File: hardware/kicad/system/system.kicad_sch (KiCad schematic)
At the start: 0 parts

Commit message: system: connected top sheet for the integrated PCB
Rebuild system.kicad_sch as the netlist-connected 5-board hierarchy
(motor_power, motor_feedback, mppt_buck, boost_v2_mill, c2000_feedback),
replacing the old block-diagram. Connectivity by global labels.

- J_ARD (Arduino), J_C2K (C2000), J_INA (PV INA219) connectors
- external screw terminals: 3-phase, motor, PV, store, load, +15V, +5V
- 17 diagnostic probe-point headers on the key nets
- single GND<->GND_MCU star tie (R_STAR 0R)
- generator tools/generators/build_system_top.py (reference; the sheet is
  now hand-maintained in the GUI)

Netlist verified: all 36 top-level connector pins match the interface
contract, no shorts, STORE/V1/LOAD buses span the right boards. Sub-sheet
.kicad_sch carry hierarchical instance data from opening the hierarchy.
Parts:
- added J_15V: +15V gate supply, symbol Connector:Screw_Terminal_01x02
- added J_3PH: 3-phase in, symbol Connector:Screw_Terminal_01x03
- added J_5V: +5V supply, symbol Connector:Screw_Terminal_01x02
- added J_ARD: Arduino Nano, symbol Connector_Generic:Conn_01x06
- added J_C2K: C2000 LaunchPad, symbol Connector_Generic:Conn_01x07
- added J_INA: PV INA219, symbol Connector_Generic:Conn_01x06
- added J_LOAD: pulsing load, symbol Connector:Screw_Terminal_01x02
- added J_MOT: DC motor, symbol Connector:Screw_Terminal_01x02
- added J_PV: PV panel, symbol Connector:Screw_Terminal_01x02
- added J_STO: 1F store, symbol Connector:Screw_Terminal_01x02
- added R_STAR: 0R, symbol Device:R
- added TP1: V1, symbol Connector:TestPoint
- added TP10: PWM_BOOST, symbol Connector:TestPoint
- added TP11: PWM_MPPT, symbol Connector:TestPoint
- added TP12: ADC_V1, symbol Connector:TestPoint
- added TP13: ADC_LOAD, symbol Connector:TestPoint
- added TP14: ADC_STORE, symbol Connector:TestPoint
- added TP15: MCU_V1, symbol Connector:TestPoint
- added TP16: PV_SDA, symbol Connector:TestPoint
- added TP17: PV_SCL, symbol Connector:TestPoint
- added TP2: STORE, symbol Connector:TestPoint
- added TP3: LOAD, symbol Connector:TestPoint
- added TP4: +5V_PWR, symbol Connector:TestPoint
- added TP5: +3V3, symbol Connector:TestPoint
- added TP6: +15V_GATE, symbol Connector:TestPoint
- added TP7: GND, symbol Connector:TestPoint
- added TP8: GND_MCU, symbol Connector:TestPoint
- added TP9: PWM_MOTOR, symbol Connector:TestPoint
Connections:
- new net +15V_GATE: J_15V.1 (Pin_1), TP6.1
- new net +3V3: J_C2K.6 (Pin_6), TP5.1
- new net +5V_PWR: J_5V.1 (Pin_1), J_ARD.5 (Pin_5), J_INA.3 (Pin_3), TP4.1
- new net 3PH_U: J_3PH.1 (Pin_1)
- new net 3PH_V: J_3PH.2 (Pin_2)
- new net 3PH_W: J_3PH.3 (Pin_3)
- new net ADC_LOAD: J_C2K.2 (Pin_2), TP13.1
- new net ADC_STORE: J_C2K.3 (Pin_3), TP14.1
- new net ADC_V1: J_C2K.1 (Pin_1), TP12.1
- new net GND: J_15V.2 (Pin_2), J_5V.2 (Pin_2), J_ARD.6 (Pin_6), J_C2K.7 (Pin_7), J_INA.4 (Pin_4), J_LOAD.2 (Pin_2), J_PV.2 (Pin_2), J_STO.2 (Pin_2), R_STAR.1, TP7.1
- new net GND_MCU: R_STAR.2, TP8.1
- new net LOAD: J_LOAD.1 (Pin_1), TP3.1
- new net MCU_V1: J_ARD.1 (Pin_1), TP15.1
- new net MOTOR_A: J_MOT.1 (Pin_1)
- new net MOTOR_B: J_MOT.2 (Pin_2)
- new net PV_BUCK_IN: J_INA.2 (Pin_2)
- new net PV_PLUS: J_INA.1 (Pin_1), J_PV.1 (Pin_1)
- new net PV_SCL: J_ARD.3 (Pin_3), J_INA.6 (Pin_6), TP17.1
- new net PV_SDA: J_ARD.2 (Pin_2), J_INA.5 (Pin_5), TP16.1
- new net PWM_BOOST: J_C2K.5 (Pin_5), TP10.1
- new net PWM_MOTOR: J_C2K.4 (Pin_4), TP9.1
- new net PWM_MPPT: J_ARD.4 (Pin_4), TP11.1
- new net STORE: J_STO.1 (Pin_1), TP2.1
- new net V1: TP1.1
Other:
- removed sheet Buck
- removed sheet Current sense
- removed sheet Feedback
- removed sheet MPPT + PV
- removed sheet Motor-drive
- removed sheet Rectifier
- added sheet C2000 Feedback (../boards/c2000_feedback/c2000_feedback.kicad_sch)
- added sheet MPPT buck (../boards/mppt_buck/mppt_buck.kicad_sch)
- added sheet Motor Feedback (../boards/motor_feedback/motor_feedback.kicad_sch)
- added sheet Motor Power (../boards/motor_power/motor_power.kicad_sch)
- sheet Boost: file ../boards/boost/boost.kicad_sch -> ../boards/boost/boost_v2_mill/boost_v2_mill.kicad_sch
- sheet Boost ports: added +15V_GATE, GND, GND_MCU, LOAD, PWM_BOOST, STORE; removed none
- note removed: "+ 3x transformer (eksterne)"
- note removed: "+ overvaagning (PC)"
- note removed: "1F LAGER"
- note removed: "3-fase"
- note removed: "5 V"
- note removed: "5 V fra lager"
- note removed: "ADC"
- note removed: "ARDUINO UNO"
- note removed: "DC-motor + AC-generator"
- note removed: "Feedback/current sense maaler V1, V2, V3 + gren-stroemme"
- note removed: "PID: V1 via motor-PWM"
- note removed: "PULSERENDE LAST"
- note removed: "PWM (PID regulerer V1 via motorfart)"
- note removed: "V1 = 15 V"
- note removed: "V2 = 10 V"
- note removed: "V3 (PV-energi bruges foerst)"
- note removed: "V3 = 5 V"
- note removed: "motorkabel (M1)"
- title: 62768 Electrical Energy Systems - samlet system -> (none)

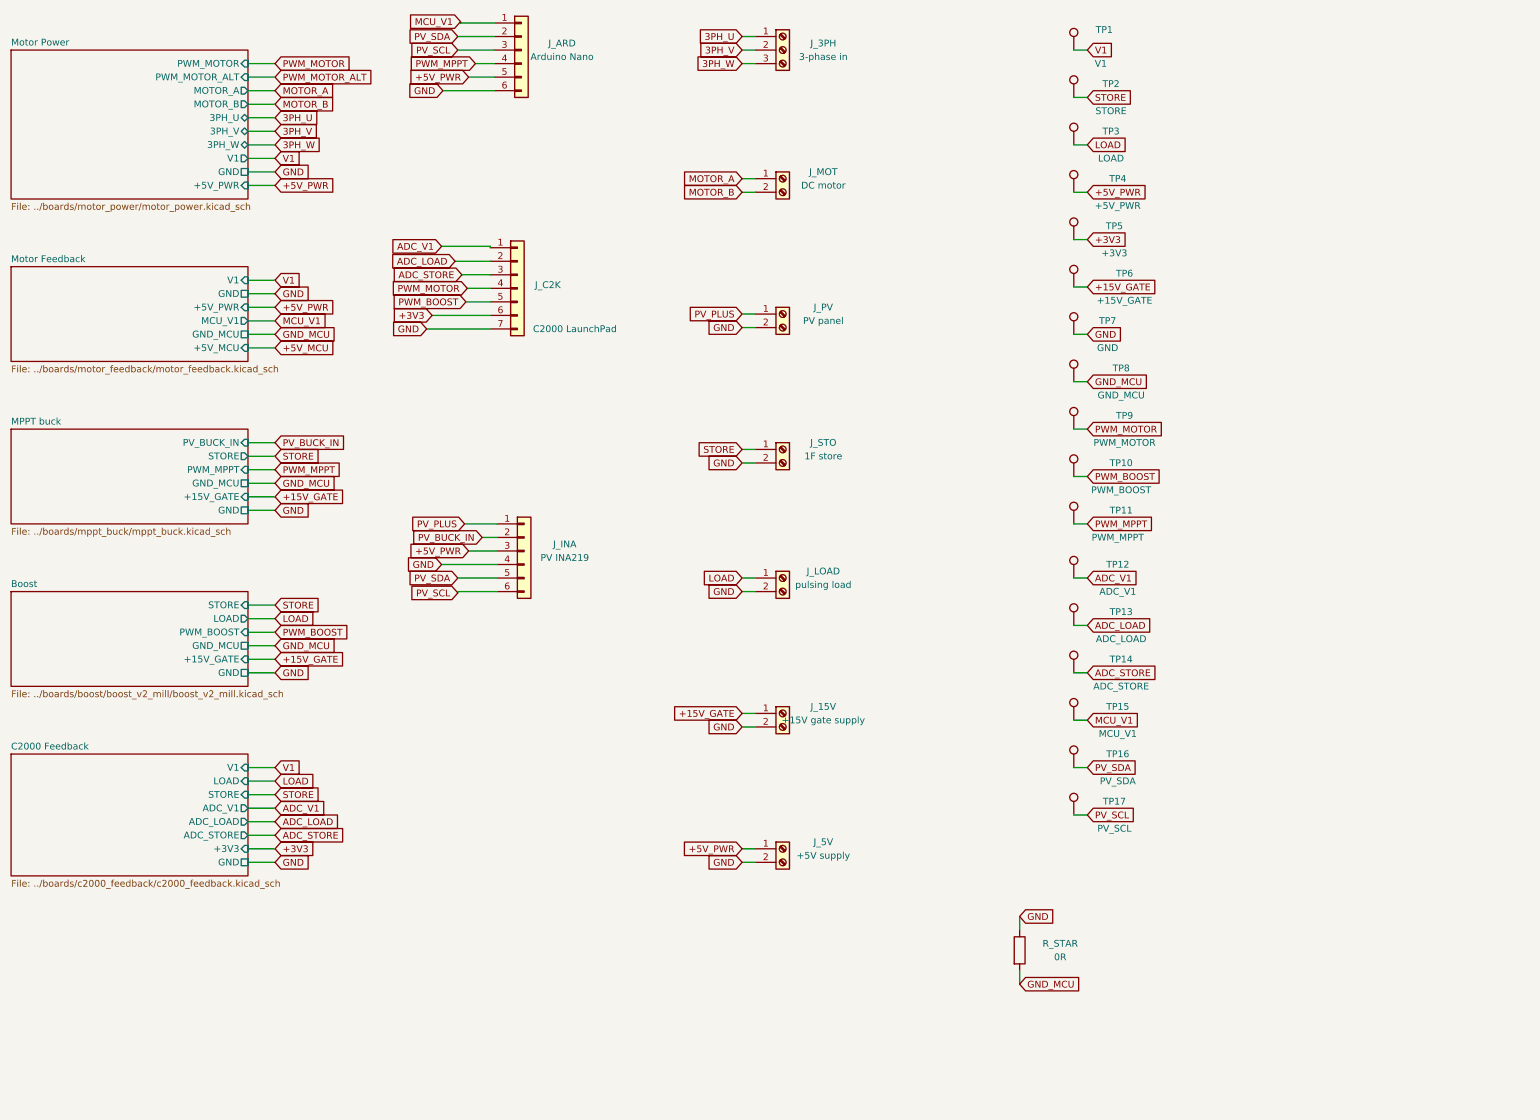
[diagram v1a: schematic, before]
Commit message: system: single edge-connector set + integrated board
- delete 22 redundant board-level I/O connectors (J201-207, J301-302,
  J401-404, J501-504, J601-605); on the monolithic board these are internal
  board-to-board nets (now copper traces) or duplicates of the top-level edge
  set. Nets carried by the hierarchical sheet pins; netlist re-verified.
- C212: real capacitor footprint, + on V1 (was a swap terminal)
- motor_feedback MCU-side powered from +5V_PWR (merged +5V_MCU)
- footprints assigned to all top-level connectors/probes (J_*, TP, R_STAR)
- system.kicad_pcb: integrated board pulled via Update-PCB-from-Schematic
- placement guide (PNG + PDF) + generator/patch scripts
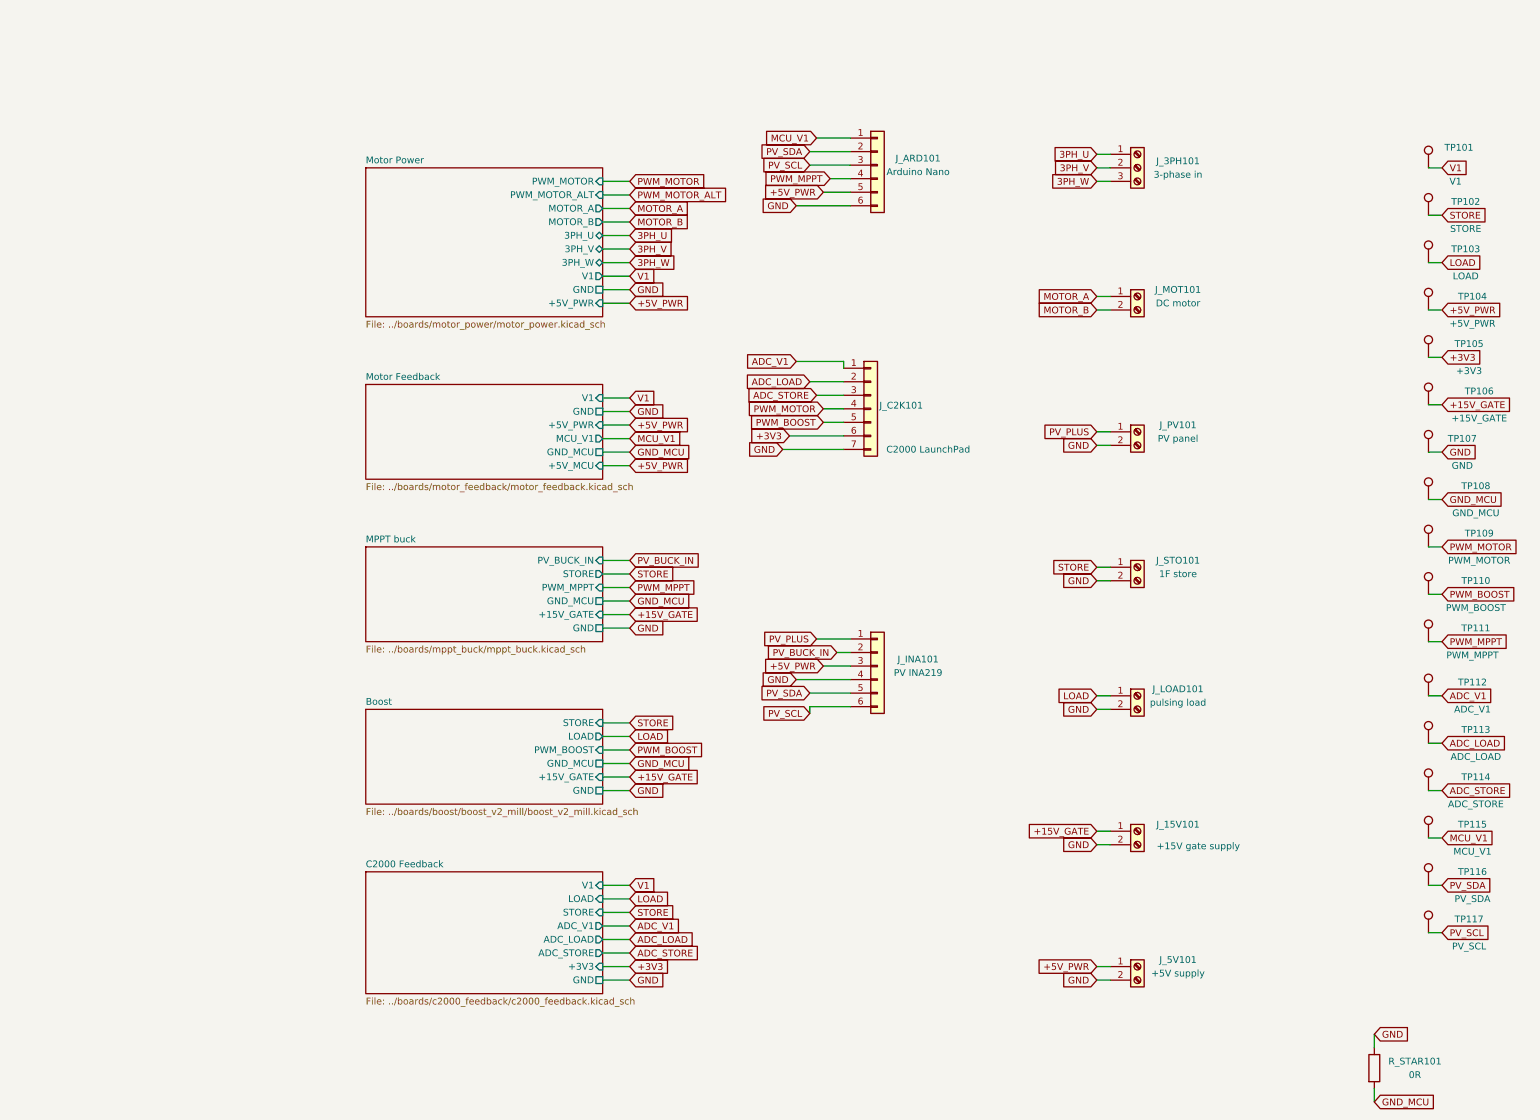
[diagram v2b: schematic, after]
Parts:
- J_15V101: renamed from J_15V; footprint (none) -> TerminalBlock:TerminalBlock_bornier-2_P5.08mm
- J_3PH101: renamed from J_3PH; footprint (none) -> TerminalBlock:TerminalBlock_bornier-3_P5.08mm
- J_5V101: renamed from J_5V; footprint (none) -> TerminalBlock:TerminalBlock_bornier-2_P5.08mm
- J_ARD101: renamed from J_ARD; footprint (none) -> Connector_PinHeader_2.54mm:PinHeader_1x06_P2.54mm_Vertical
- J_C2K101: renamed from J_C2K; footprint (none) -> Connector_PinHeader_2.54mm:PinHeader_1x07_P2.54mm_Vertical
- J_INA101: renamed from J_INA; footprint (none) -> Connector_PinHeader_2.54mm:PinHeader_1x06_P2.54mm_Vertical
- J_LOAD101: renamed from J_LOAD; footprint (none) -> TerminalBlock:TerminalBlock_bornier-2_P5.08mm
- J_MOT101: renamed from J_MOT; footprint (none) -> TerminalBlock:TerminalBlock_bornier-2_P5.08mm
- J_PV101: renamed from J_PV; footprint (none) -> TerminalBlock:TerminalBlock_bornier-2_P5.08mm
- J_STO101: renamed from J_STO; footprint (none) -> TerminalBlock:TerminalBlock_bornier-2_P5.08mm
- R_STAR101: renamed from R_STAR; footprint (none) -> Resistor_THT:R_Axial_DIN0207_L6.3mm_D2.5mm_P7.62mm_Horizontal
- TP101: renamed from TP1; footprint (none) -> Connector_PinHeader_2.54mm:PinHeader_1x01_P2.54mm_Vertical
- TP102: renamed from TP2; footprint (none) -> Connector_PinHeader_2.54mm:PinHeader_1x01_P2.54mm_Vertical
- TP103: renamed from TP3; footprint (none) -> Connector_PinHeader_2.54mm:PinHeader_1x01_P2.54mm_Vertical
- TP104: renamed from TP4; footprint (none) -> Connector_PinHeader_2.54mm:PinHeader_1x01_P2.54mm_Vertical
- TP105: renamed from TP5; footprint (none) -> Connector_PinHeader_2.54mm:PinHeader_1x01_P2.54mm_Vertical
- TP106: renamed from TP6; footprint (none) -> Connector_PinHeader_2.54mm:PinHeader_1x01_P2.54mm_Vertical
- TP107: renamed from TP7; footprint (none) -> Connector_PinHeader_2.54mm:PinHeader_1x01_P2.54mm_Vertical
- TP108: renamed from TP8; footprint (none) -> Connector_PinHeader_2.54mm:PinHeader_1x01_P2.54mm_Vertical
- TP109: renamed from TP9; footprint (none) -> Connector_PinHeader_2.54mm:PinHeader_1x01_P2.54mm_Vertical
- TP110: renamed from TP10; footprint (none) -> Connector_PinHeader_2.54mm:PinHeader_1x01_P2.54mm_Vertical
- TP111: renamed from TP11; footprint (none) -> Connector_PinHeader_2.54mm:PinHeader_1x01_P2.54mm_Vertical
- TP112: renamed from TP12; footprint (none) -> Connector_PinHeader_2.54mm:PinHeader_1x01_P2.54mm_Vertical
- TP113: renamed from TP13; footprint (none) -> Connector_PinHeader_2.54mm:PinHeader_1x01_P2.54mm_Vertical
- TP114: renamed from TP14; footprint (none) -> Connector_PinHeader_2.54mm:PinHeader_1x01_P2.54mm_Vertical
- TP115: renamed from TP15; footprint (none) -> Connector_PinHeader_2.54mm:PinHeader_1x01_P2.54mm_Vertical
- TP116: renamed from TP16; footprint (none) -> Connector_PinHeader_2.54mm:PinHeader_1x01_P2.54mm_Vertical
- TP117: renamed from TP17; footprint (none) -> Connector_PinHeader_2.54mm:PinHeader_1x01_P2.54mm_Vertical
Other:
- moved on the sheet: J_15V101, J_3PH101, J_5V101, J_ARD101, J_C2K101, J_INA101, J_LOAD101, J_MOT101, J_PV101, J_STO101, R_STAR101, TP101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

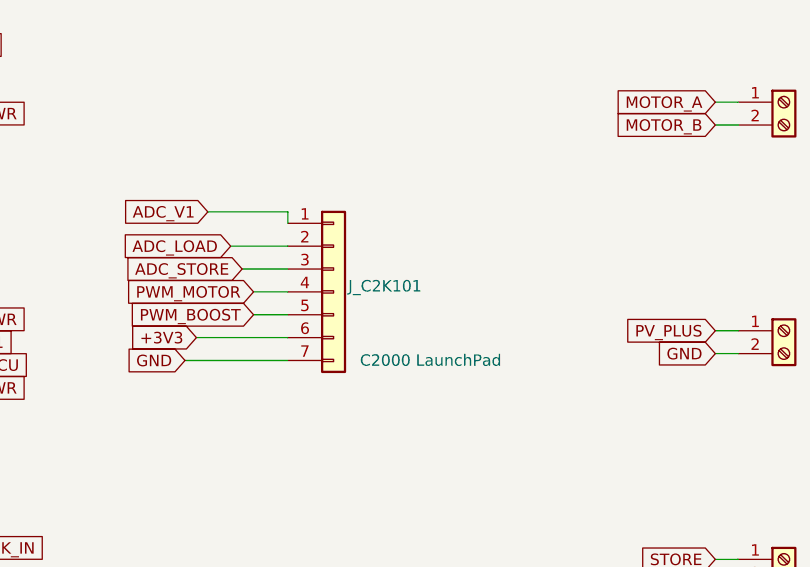
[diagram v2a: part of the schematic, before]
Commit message: system PCB: routing prep (track 1.0, GND pour both layers) + board/CAM updates
system board:
- fix Default netclass track 0.9 -> 1.0 mm (was below min_track_width, every
  trace would have failed DRC); clearance 1.0, via 2.4/1.0 in .kicad_pro + board
- pour GND on F.Cu and B.Cu (edge inset 0.5 mm, solid pad tie)
- routing tooling: route_prep (netclass+pour), export_dsn_noplane (route GND as
  tracks; Freerouting 1.9.0 chokes on full-board planes), route_finish (SES
  import + refill + sparse GND stitching), inspect_system

srm-cam: bump submodule to double-sided support (90 rotation, bottom-side bed
leveling, GUI ruler/STOP/probe-grid, run-time estimator)

production: rename boost_v2_mill nc -> board_*, add drive_circuit trace rework
boards: buck_v2, current_sense, c2000_feedback edits; BOM + AD3 lab-guide
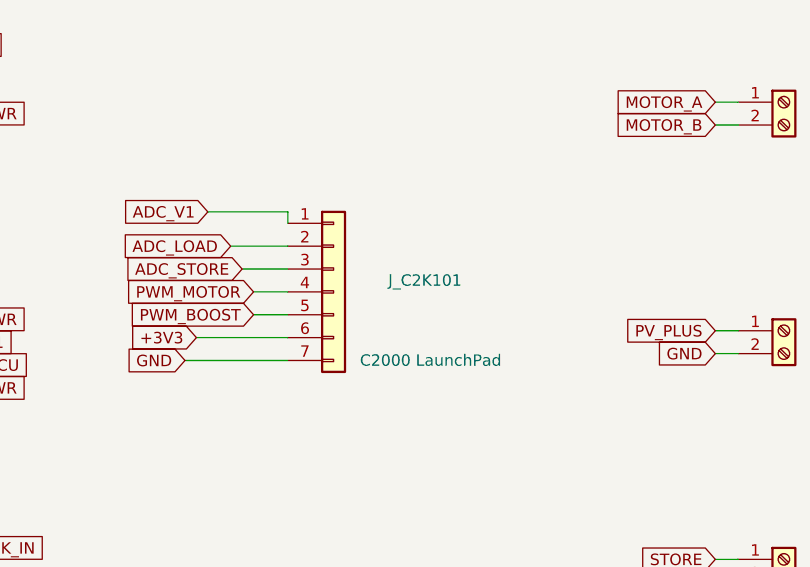
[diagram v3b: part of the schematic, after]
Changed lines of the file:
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@@
 		(dnp no)
 		(property "Reference" "J_C2K101"
-			(at 197.485 97.155 0)
+			(at 201.93 96.52 0)
 			(show_name no)
 			(do_not_autoplace no)
